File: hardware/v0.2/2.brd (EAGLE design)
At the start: 54.9 x 27.5 mm, 26 parts, among them IC2 STM32F10XCXT6, U1 ADXL345"

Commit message: modify pcb design
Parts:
- removed R12, R13, R14, R15: 470R, rcl:R0603
- added C3: 10uF, SparkFun-Capacitors:EIA3216
- added LED3, LED4, LED5, LED6, LED7, LED8: (no value), SparkFun-LED:LED-1206
- added R1, R2, R6, R7, R8, R9: 10K, rcl:R0603
- added S1: SWITCH-MOMENTARY-2-SMD-1101NE, SparkFun-Electromechanical:TACTILE-SWITCH-1101NE
- LED1, LED2: value LED-TRICOLOR-5050NO_IC -> (none); device SparkFun-LED:LED-TRICOLOR-5050 -> SparkFun-LED:LED-1206
- R10, R11: value 470R -> 10K
- moved C4 51.8 mm to (49.5, 7.70)
- moved C1 48.0 mm to (49.0, 2.90)
- moved R10 45.1 mm to (50.7, 15.7)
- moved C2 39.9 mm to (35.8, 13.4)
- moved LED2 39.1 mm to (8.00, 15.6)
- moved R11 37.3 mm to (42.6, 21.7)
- moved U1 28.9 mm to (44.0, 4.50), turned to 270 degrees
- moved JP5 27.6 mm to (35.0, 2.00), turned to 180 degrees
- moved JP4 27.1 mm to (24.2, 25.8)
- moved JP1 24.9 mm to (11.5, 25.3)
- moved F1 24.0 mm to (7.00, 1.80)
- moved R5 23.7 mm to (23.4, 1.70)
- moved R3 16.0 mm to (27.7, 1.70)
- moved LED1 10.6 mm to (17.6, 21.9)
- moved C8 1.72 mm to (24.1, 18.7)
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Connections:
- removed net LED1_B: LED1.4
- removed net LED1_G: LED1.6
- removed net LED1_R: LED1.5
- removed net LED2_B: LED2.4
- removed net LED2_G: LED2.6
- removed net LED2_R: LED2.5
- removed net N$10: LED1.1, R11.2
- removed net N$11: LED1.2, R12.2
- removed net N$12: LED2.3, R13.2
- removed net N$13: LED2.1, R14.2
- removed net N$14: LED2.2, R15.2
- removed net N$8: LED1.3, R10.2
- new net N$3: R6.1, R7.2
- new net N$4: R8.1, R9.2
- net 3.3V: now also C3.A, S1.P$1; no longer R10.1, R11.1, R12.1, R13.1, R14.1, R15.1
- net GND: now also C3.C
- net N$2: now also S1.P$2
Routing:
- net GND: track 38.6 -> 0.00 mm, vias 3 -> 0
- net USART1_TX: track 30.1 -> 0.00 mm, vias 1 -> 0
- net USART1_RX: track 28.0 -> 0.00 mm, vias 1 -> 0
- net 3.3V: track 21.2 -> 0.00 mm
- net BOOT0: track 20.1 -> 0.00 mm
- net RESET: track 8.12 -> 0.00 mm
- net N$13: track 3.76 -> 0.00 mm
- net N$10: track 3.64 -> 0.00 mm
- net N$8: track 3.58 -> 0.00 mm
- net N$14: track 3.17 -> 0.00 mm
- net N$2: track 3.13 -> 0.00 mm
- net N$12: track 3.03 -> 0.00 mm
- net N$11: track 2.65 -> 0.00 mm
- net WAKEUP: track 1.00 -> 0.00 mm
- net LED1_R: track 0.88 -> 0.00 mm
- removed copper zone on layer 1, net GND
- removed copper zone on layer 16, net GND
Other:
- board text removed: "ON/OFF"

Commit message: Updated V2 PCB design
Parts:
- removed C11: 4.7u, rcl:C0603K
- removed IC2: STM32F10XCXT6, stm32:TQFP48
- removed JP5: M02PTH, SparkFun-Connectors:1X02
- removed LED5, LED6, LED7, LED8: (no value), SparkFun-LED:LED-1206
- added BL1: (no value), digital-toy:SOT23-5
- added C6: 10u, rcl:C0603K
- added C7: 0.1u, rcl:C0603K
- added D1: BAT20JFILM, SparkFun-DiscreteSemi:SOD-323
- added IC1: STM32F10XCXT6, stm32:TQFP48
- added JP3: (no value), SparkFun-Connectors:1X04
- added L1: (no value), SparkFun-Passives:VLF4012A
- C1, C2: value 0.1u -> 10uF; device rcl:C0603K -> SparkFun-Capacitors:EIA3216
- C10: value 0.1u -> 4.7u
- C3, C4: value 10uF -> 0.1u; device SparkFun-Capacitors:EIA3216 -> rcl:C0603K
- C5: value 10u -> 100uF; device rcl:C0603K -> SparkFun-Capacitors:EIA3528
- JP1: device SparkFun-Connectors:1X04 -> SparkFun-Connectors:1X03
- JP4: value (none) -> M02PTH; device SparkFun-Connectors:1X03 -> SparkFun-Connectors:1X02
- LED1, LED2: value (none) -> LED-TRICOLOR-5050NO_IC; device SparkFun-LED:LED-1206 -> SparkFun-LED:LED-TRICOLOR-5050
- R1, R2, R3, R4, R5, R6, R8, R9: value 10K -> 270
- moved C1 42.6 mm to (6.40, 2.80)
- moved LED2 41.0 mm to (49.0, 14.0)
- moved C4 34.2 mm to (15.8, 13.6)
- moved JP1 32.1 mm to (34.0, 2.40)
- moved R6 29.4 mm to (43.0, 15.0)
- moved R9 29.1 mm to (23.0, 2.00)
- moved C5 28.0 mm to (7.80, 24.0), turned to 270 degrees
- moved R5 25.5 mm to (43.0, 18.0)
- moved U1 24.1 mm to (21.8, 14.0), turned to 90 degrees
- moved LED3 24.1 mm to (28.0, 25.0)
- moved R1 22.9 mm to (3.40, 9.40), turned to 180 degrees
- moved R11 22.7 mm to (26.2, 6.00)
- moved R10 22.3 mm to (29.0, 21.0)
- moved R3 21.7 mm to (7.40, 9.40)
- moved R8 21.3 mm to (23.0, 25.0)
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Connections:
- new net 2.8V: C1.A, C10.1, C2.A, C3.1, C4.1, C7.1, C8.1, C9.1, F1.1, IC1.1, IC1.24, IC1.36, IC1.48, IC1.9, JP3.1, JP4.1, L1.P$1, R11.1, S1.P$1, U1.1, U1.6
- new net LED1_B: LED1.4
- new net LED1_G: LED1.6
- new net LED1_R: LED1.5
- new net LED2_B: LED2.4
- new net LED2_G: LED2.6
- new net LED2_R: LED2.5
- new net LED_EN: BL1.1
- new net N$10: LED2.1, R5.2
- new net N$11: LED2.2, R6.2
- new net N$12: BL1.5, D1.2, L1.P$2
- new net N$6: LED1.3, R1.2
- new net N$7: LED1.1, R2.2
- new net N$8: LED1.2, R3.2
- new net N$9: LED2.3, R4.2
- net 3.3V: now also BL1.2, C5.A, D1.1, R1.1, R2.1, R4.1, R5.1, R6.1, R8.1, R9.1; no longer C1.1, C10.1, C11.1, C2.1, C3.A, C4.A, C8.1, C9.1, F1.1, IC2.1, IC2.24, IC2.36, IC2.48, IC2.9, JP1.1, JP5.1, S1.P$1, U1.1
- net BOOT0: now also IC1.44, JP4.2, R7.2; no longer IC2.44, JP5.2, R5.2
- net GND: now also BL1.4, C1.C, C2.C, C3.2, C4.2, C5.C, C6.2, C7.2, IC1.23, IC1.35, IC1.47, IC1.8, JP1.3, JP3.4, R10.2, R7.1; no longer C1.2, C11.2, C2.2, C3.C, C4.C, C5.2, IC2.23, IC2.35, IC2.47, IC2.8, JP1.4, JP4.3, R4.2, R5.1
- net N$2: now also IC1.20, R10.1; no longer IC2.20, R4.1
- net N$3: now also LED4.A, R9.2; no longer R6.1, R7.2
- net N$4: now also LED3.A, R8.2; no longer R8.1, R9.2
- net RESET: now also C6.1, IC1.7, R11.2; no longer C5.1, IC2.7, R3.2
- net SWCLK: now also IC1.37, JP3.3; no longer IC2.37, JP1.3
- net SWDIO: now also IC1.34, JP3.2; no longer IC2.34, JP1.2
- net USART1_RX: now also IC1.31, JP1.2; no longer IC2.31, JP4.2
- net USART1_TX: now also IC1.30, JP1.1; no longer IC2.30, JP4.1
- net WAKEUP: now also IC1.10; no longer IC2.10
- net XL345_CS: now also IC1.14; no longer IC2.14
- net XL345_INT: now also IC1.13; no longer IC2.13
- net XL345_MISO: now also IC1.16; no longer IC2.16
- net XL345_MOSI: now also IC1.17; no longer IC2.17
- net XL345_SCK: now also IC1.15; no longer IC2.15
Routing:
- net 3.3V: track 0.00 -> 6.00 mm
- net N$10: track 0.00 -> 3.70 mm
- net N$11: track 0.00 -> 3.16 mm
- net N$9: track 0.00 -> 2.87 mm
- net N$4: track 0.00 -> 2.65 mm
- net N$3: track 0.00 -> 2.65 mm
- net GND: track 0.00 -> 0.80 mm
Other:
- board text removed: "CLK"
- board text removed: "G"
- board text removed: "GND"
- board text removed: "IO"
- board text removed: "RX"
- board text removed: "TX"
- board text removed: "UPDATE"
- board text removed: "V"
- board text removed: "VDD"

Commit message: nearly finish PCB design
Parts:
- moved R10 17.6 mm to (46.6, 20.2), turned to 90 degrees
- moved R11 14.3 mm to (30.6, 19.6), turned to 180 degrees
- moved R1 13.5 mm to (16.2, 5.20), turned to 0 degrees
- moved C9 12.8 mm to (34.8, 6.40), turned to 270 degrees
- moved C10 10.0 mm to (34.6, 18.6), turned to 0 degrees
- moved R3 9.02 mm to (16.2, 7.40), turned to 0 degrees
- moved C6 8.41 mm to (30.6, 21.8), turned to 180 degrees
- moved D1 6.01 mm to (8.30, 24.6)
- moved JP4 5.80 mm to (34.0, 24.6), turned to 0 degrees
- moved BL1 5.20 mm to (3.40, 24.8)
- moved C3 5.20 mm to (16.2, 21.2), turned to 180 degrees
- moved L1 4.62 mm to (3.60, 20.0), turned to 90 degrees
- moved R4 4.44 mm to (38.9, 13.7)
- moved R6 4.20 mm to (38.9, 15.9)
- moved R5 4.10 mm to (38.9, 18.1)
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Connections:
- removed net XL345_INT: IC1.13, U1.8
- new net LED3: IC1.12, LED3.C
- new net LED4: IC1.28, LED4.C
- new net N$13: IC1.19
- net 3.3V: now also LED1.1, LED1.2, LED1.3; no longer R1.1, R2.1, R3.1
- net LED1_B: now also IC1.27, R1.2; no longer LED1.4
- net LED1_G: now also IC1.25, R2.2; no longer LED1.6
- net LED1_R: now also IC1.26, R3.2; no longer LED1.5
- net LED2_B: now also IC1.41
- net LED2_G: now also IC1.43
- net LED2_R: now also IC1.42
- net N$6: now also LED1.4, R1.1; no longer LED1.3, R1.2
- net N$7: now also LED1.6, R2.1; no longer LED1.1, R2.2
- net N$8: now also LED1.5, R3.1; no longer LED1.2, R3.2
- net WAKEUP: now also U1.8; no longer U1.9
- net XL345_CS: now also IC1.18; no longer IC1.14
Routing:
- net GND: track 0.80 -> 240.3 mm, vias 0 -> 7
- net 2.8V: track 0.00 -> 144.1 mm, vias 0 -> 2
- net 3.3V: track 6.00 -> 83.6 mm, vias 0 -> 4
- net N$2: track 0.00 -> 37.7 mm, vias 0 -> 2
- net SWDIO: track 0.00 -> 22.5 mm, vias 0 -> 1
- net LED2_G: track 0.00 -> 20.5 mm
- net LED2_R: track 0.00 -> 19.6 mm
- net LED2_B: track 0.00 -> 18.4 mm
- net SWCLK: track 0.00 -> 18.0 mm
- net BOOT0: track 0.00 -> 14.3 mm
- net LED1_B: track 0.00 -> 13.8 mm, vias 0 -> 2
- net LED3: track 0.00 -> 12.8 mm, vias 0 -> 2
- net LED1_R: track 0.00 -> 12.8 mm, vias 0 -> 2
- net LED1_G: track 0.00 -> 11.3 mm, vias 0 -> 2
- net XL345_SCK: track 0.00 -> 10.8 mm
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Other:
- board size 54.9 x 27.5 mm -> 55 x 27.5 mm
- board text added: "2014-3-20 V0.2"
- board text removed: "2014-2-10 V0.1"

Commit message: finish version 0.2 pcb design
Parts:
- C1: value 10uF -> 22uF
- L1: value (none) -> 22uh
- moved LED4 0.30 mm to (28.0, 2.50)
- moved R9 0.30 mm to (23.0, 2.50)
- renumbered BL1 to IC3, U1 to IC2
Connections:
- removed net N$13: IC1.19
- net LED2_B: now also IC1.40; no longer IC1.41
- net LED3: now also IC1.45; no longer IC1.12
- net LED_EN: now also IC1.13
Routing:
- net LED_EN: track 0.00 -> 26.4 mm, vias 0 -> 2
- net LED3: track 12.8 -> 16.6 mm
- net GND: track 240.3 -> 241.7 mm, vias 7 -> 8
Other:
- board text added: "G"
- board text added: "GND"
- board text added: "Rx"
- board text added: "SWDCLK"
- board text added: "SWDIO"
- board text added: "Tx"
- board text added: "UPDATE"
- board text added: "V"
- board text added: "VCC"
- board text added: "X"
- board text added: "Y"
- board text added: "Z"

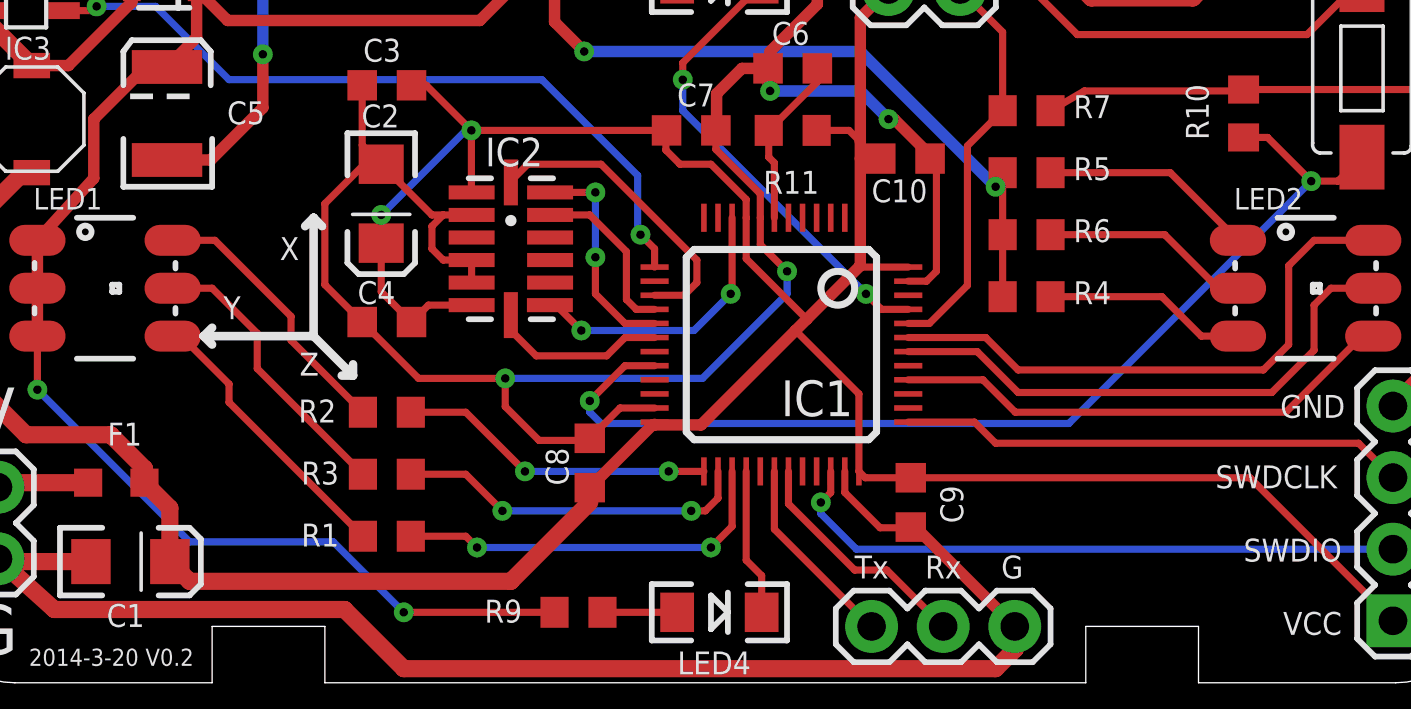
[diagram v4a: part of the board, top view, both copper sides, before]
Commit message: update schematic for clearance
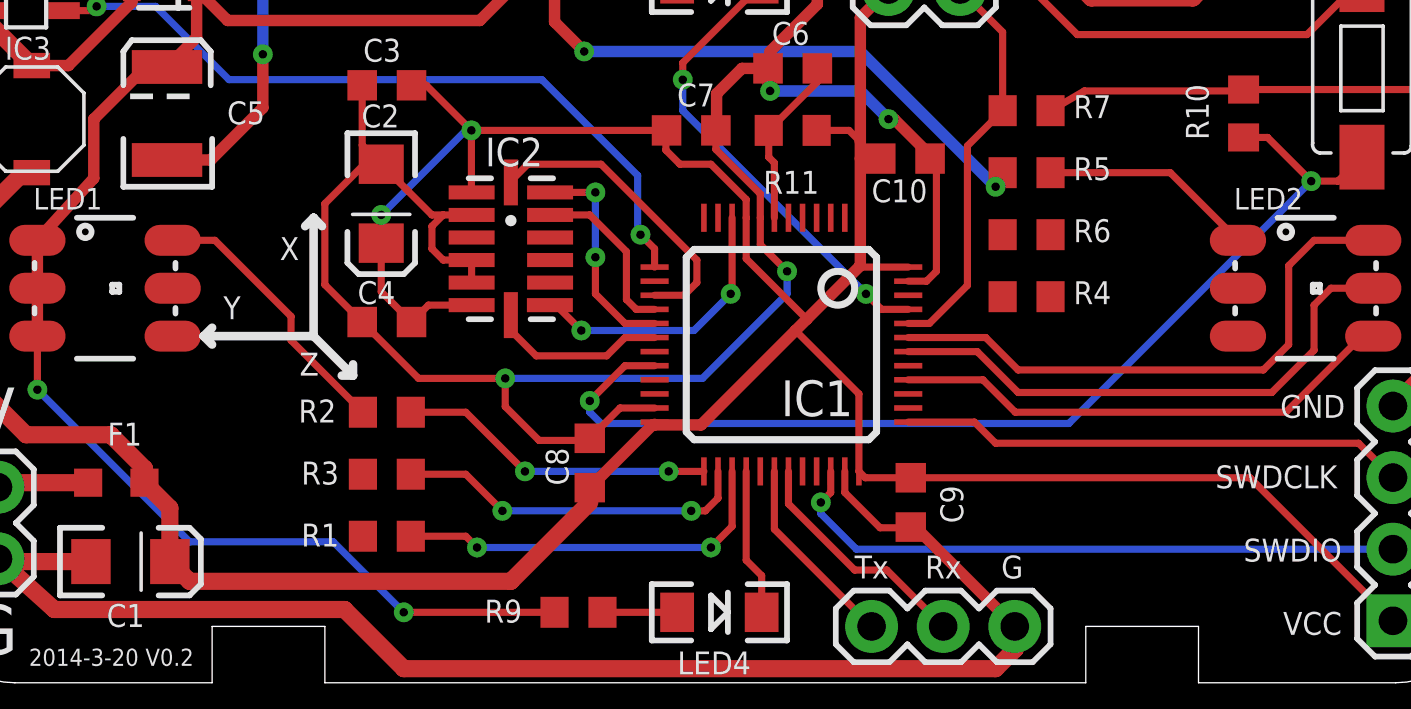
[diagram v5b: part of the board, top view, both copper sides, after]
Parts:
- R1, R4: value 270 -> 300
- R2, R3, R5, R6, R8, R9: value 270 -> 470
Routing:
- net N$11: track 10.2 -> 0.00 mm
- net N$9: track 10.1 -> 0.00 mm
- net N$8: track 7.44 -> 0.00 mm
- net N$6: track 7.23 -> 0.00 mm
- net 3.3V: track 83.4 -> 79.0 mm
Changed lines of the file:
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@@
 <attribute name="VALUE" x="26.984" y="0.722" size="0.4064" layer="27"/>
 </element>
-<element name="R8" library="rcl" package="R0603" value="270" x="23" y="24.8" smashed="yes">
+<element name="R8" library="rcl" package="R0603" value="470" x="23" y="24.8" smashed="yes">
 <attribute name="NAME" x="22.265" y="26.135" size="0.8128" layer="25"/>
 </element>
-<element name="R9" library="rcl" package="R0603" value="270" x="23" y="2.5" smashed="yes">
+<element name="R9" library="rcl" package="R0603" value="470" x="23" y="2.5" smashed="yes">
 <attribute name="NAME" x="19.665" y="2.135" size="0.8128" layer="25"/>
 </element>
@@
 <attribute name="NAME" x="11.87" y="20.63" size="0.8128" layer="25" rot="R180"/>
 </element>
-<element name="R1" library="rcl" package="R0603" value="270" x="16.2" y="5.2" smashed="yes">
+<element name="R1" library="rcl" package="R0603" value="300" x="16.2" y="5.2" smashed="yes">
 <attribute name="NAME" x="13.165" y="4.835" size="0.8128" layer="25"/>
 </element>
-<element name="R2" library="rcl" package="R0603" value="270" x="16.2" y="9.6" smashed="yes">
+<element name="R2" library="rcl" package="R0603" value="470" x="16.2" y="9.6" smashed="yes">
 <attribute name="NAME" x="13.065" y="9.235" size="0.8128" layer="25"/>
 </element>
-<element name="R3" library="rcl" package="R0603" value="270" x="16.2" y="7.4" smashed="yes">
+<element name="R3" library="rcl" package="R0603" value="470" x="16.2" y="7.4" smashed="yes">
 <attribute name="NAME" x="13.165" y="7.035" size="0.8128" layer="25"/>
 </element>
-<element name="R4" library="rcl" package="R0603" value="270" x="38.9" y="13.7" smashed="yes">
+<element name="R4" library="rcl" package="R0603" value="300" x="38.9" y="13.7" smashed="yes">
 <attribute name="NAME" x="40.565" y="13.435" size="0.8128" layer="25"/>
 </element>
-<element name="R5" library="rcl" package="R0603" value="270" x="38.9" y="18.1" smashed="yes">
+<element name="R5" library="rcl" package="R0603" value="470" x="38.9" y="18.1" smashed="yes">
 <attribute name="NAME" x="40.565" y="17.835" size="0.8128" layer="25"/>
 </element>
-<element name="R6" library="rcl" package="R0603" value="270" x="38.9" y="15.9" smashed="yes">
+<element name="R6" library="rcl" package="R0603" value="470" x="38.9" y="15.9" smashed="yes">
 <attribute name="NAME" x="40.565" y="15.635" size="0.8128" layer="25"/>
 </element>
@@
 <wire x1="26.1" y1="19.575" x2="26.125" y2="19.6" width="0.254" layer="1"/>
 </signal>
-<signal name="N$9">
-<contactref element="R4" pad="2"/>
-<contactref element="LED2" pad="3"/>
-<wire x1="39.75" y1="13.7" x2="43.7" y2="13.7" width="0.254" layer="1"/>
-<wire x1="43.7" y1="13.7" x2="45.1" y2="12.3" width="0.254" layer="1"/>
-<wire x1="45.1" y1="12.3" x2="46.4" y2="12.3" width="0.254" layer="1"/>
-</signal>
 <signal name="N$10">
 <contactref element="R5" pad="2"/>
@@
 <wire x1="44" y1="18.1" x2="46.4" y2="15.7" width="0.254" layer="1"/>
 </signal>
-<signal name="N$11">
-<contactref element="R6" pad="2"/>
-<contactref element="LED2" pad="2"/>
-<wire x1="39.75" y1="15.9" x2="43.8" y2="15.9" width="0.254" layer="1"/>
-<wire x1="43.8" y1="15.9" x2="45.7" y2="14" width="0.254" layer="1"/>
-<wire x1="45.7" y1="14" x2="46.4" y2="14" width="0.254" layer="1"/>
-</signal>
 <signal name="3.3V">
-<contactref element="R6" pad="1"/>
 <contactref element="R5" pad="1"/>
-<contactref element="R4" pad="1"/>
 <contactref element="IC3" pad="2"/>
 <contactref element="C5" pad="A"/>
@@
 <wire x1="37.8" y1="17.6" x2="38.3" y2="18.1" width="0.254" layer="1"/>
 <wire x1="38.3" y1="18.1" x2="38.05" y2="18.1" width="0.254" layer="1"/>
-<wire x1="38.05" y1="18.1" x2="38.05" y2="15.9" width="0.254" layer="1"/>
-<wire x1="38.05" y1="15.9" x2="38.05" y2="13.7" width="0.254" layer="1"/>
 <wire x1="10.55" y1="23.5" x2="19.5" y2="23.5" width="0.4064" layer="1"/>
 <wire x1="19.5" y1="23.5" x2="20.5" y2="24.5" width="0.4064" layer="1"/>
@@
 <via x="16.8" y="2.5" extent="1-16" drill="0.3"/>
 <wire x1="16.8" y1="2.5" x2="22.15" y2="2.5" width="0.254" layer="1"/>
+<contactref element="R4" pad="1"/>
+<contactref element="R6" pad="1"/>
+<wire x1="37.8" y1="17.6" x2="38.05" y2="15.9" width="0" layer="19" extent="1-1"/>
+<wire x1="38.05" y1="13.7" x2="38.05" y2="15.9" width="0" layer="19" extent="1-1"/>
 </signal>
 <signal name="N$12">
@@
 <wire x1="23.85" y1="24.8" x2="26.5" y2="24.8" width="0.254" layer="1"/>
 </signal>
-<signal name="N$6">
-<contactref element="R1" pad="1"/>
-<contactref element="LED1" pad="4"/>
-<wire x1="8.6" y1="12.3" x2="8.9" y2="12.3" width="0.254" layer="1"/>
-<wire x1="8.9" y1="12.3" x2="10.6" y2="10.6" width="0.254" layer="1"/>
-<wire x1="10.6" y1="10.6" x2="10.6" y2="9.95" width="0.254" layer="1"/>
-<wire x1="10.6" y1="9.95" x2="15.35" y2="5.2" width="0.254" layer="1"/>
-</signal>
 <signal name="N$7">
 <contactref element="R2" pad="1"/>
@@
 <wire x1="12.8" y1="13" x2="12.8" y2="12.15" width="0.254" layer="1"/>
 <wire x1="12.8" y1="12.15" x2="15.35" y2="9.6" width="0.254" layer="1"/>
-</signal>
-<signal name="N$8">
-<contactref element="R3" pad="1"/>
-<contactref element="LED1" pad="5"/>
-<wire x1="8.6" y1="14" x2="10" y2="14" width="0.254" layer="1"/>
-<wire x1="10" y1="14" x2="11.6" y2="12.4" width="0.254" layer="1"/>
-<wire x1="11.6" y1="12.4" x2="11.6" y2="11.15" width="0.254" layer="1"/>
-<wire x1="11.6" y1="11.15" x2="15.35" y2="7.4" width="0.254" layer="1"/>
 </signal>
 <signal name="LED1_G">
@@
 <wire x1="28.95" y1="4.35" x2="28.95" y2="7.5" width="0.254" layer="1"/>
 </signal>
+<signal name="N$6">
+<contactref element="R4" pad="2"/>
+<contactref element="LED2" pad="3"/>
+<wire x1="39.75" y1="13.7" x2="46.4" y2="12.3" width="0" layer="19" extent="1-1"/>
+</signal>
+<signal name="N$8">
+<contactref element="LED2" pad="2"/>
+<contactref element="R6" pad="2"/>
+<wire x1="39.75" y1="15.9" x2="46.4" y2="14" width="0" layer="19" extent="1-1"/>
+</signal>
+<signal name="N$9">
+<contactref element="R1" pad="1"/>
+<contactref element="LED1" pad="4"/>
+<wire x1="8.6" y1="12.3" x2="15.35" y2="5.2" width="0" layer="19" extent="1-1"/>
+</signal>
+<signal name="N$11">
+<contactref element="LED1" pad="5"/>
+<contactref element="R3" pad="1"/>
+<wire x1="15.35" y1="7.4" x2="8.6" y2="14" width="0" layer="19" extent="1-1"/>
+</signal>
 </signals>
